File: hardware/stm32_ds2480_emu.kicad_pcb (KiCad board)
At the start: 2 copper layers, 31 x 25.5 mm, 26 parts, among them J1 USB_B_Micro, J2 SWD, J3 Pull-Up, J4 OW, Q1 SI2302CDS, SW1 BOOT, U1 AP2204K-3.3, U2 STM32F042F6Px

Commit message: Firmware added
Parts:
- moved J2 7.58 mm to (129.0, 95.2), turned to 270 degrees
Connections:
- J2 pad 2: /SYS_SWCLK -> /SYS_SWDIO
- J2 pad 3: /SYS_SWDIO -> /SYS_SWCLK
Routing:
- net +3V3: track 56.1 -> 52.1 mm, vias 3 -> 4
- net GND: track 86.5 -> 85.4 mm
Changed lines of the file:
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@@
     (thickness 1.6)
     (drawings 12)
-    (tracks 175)
+    (tracks 174)
     (zones 0)
     (modules 26)
@@
   )
   (module Connector_PinHeader_2.54mm:PinHeader_1x04_P2.54mm_Vertical placed (layer F.Cu)
-    (at 121.42 95.25 90)
+    (at 129 95.25 270)
     (descr "Through hole straight pin header, 1x04, 2.54mm pitch, single row")
     (tags "Through hole pin header THT 1x04 2.54mm single row")
-    (fp_text reference J2 (at 0 -2.33 90) (layer F.SilkS) hide
-      (effects (font (size 1 1) (thickness 0.15)))
-    )
-    (fp_text value SWD (at 0 9.95 90) (layer F.Fab) hide
-      (effects (font (size 1 1) (thickness 0.15)))
-    )
-    (fp_text user %R (at 0 3.81 180) (layer F.Fab)
+    (fp_text reference J2 (at 0 -2.33 270) (layer F.SilkS) hide
+      (effects (font (size 1 1) (thickness 0.15)))
+    )
+    (fp_text value SWD (at 0 9.95 270) (layer F.Fab) hide
+      (effects (font (size 1 1) (thickness 0.15)))
+    )
+    (fp_text user %R (at 0 3.81) (layer F.Fab)
       (effects (font (size 1 1) (thickness 0.15)))
     )
@@
     (fp_line (start 1.27 -1.27) (end 1.27 8.89) (layer F.Fab) (width 0.1))
     (fp_line (start -0.635 -1.27) (end 1.27 -1.27) (layer F.Fab) (width 0.1))
-    (pad 4 thru_hole oval (at 0 7.62 90) (size 1.7 1.7) (drill 1) (layers *.Cu *.Mask)
-      (net 2 GND))
-    (pad 3 thru_hole oval (at 0 5.08 90) (size 1.7 1.7) (drill 1) (layers *.Cu *.Mask)
+    (pad 4 thru_hole oval (at 0 7.62 270) (size 1.7 1.7) (drill 1) (layers *.Cu *.Mask)
+      (net 2 GND))
+    (pad 3 thru_hole oval (at 0 5.08 270) (size 1.7 1.7) (drill 1) (layers *.Cu *.Mask)
+      (net 9 /SYS_SWCLK))
+    (pad 2 thru_hole oval (at 0 2.54 270) (size 1.7 1.7) (drill 1) (layers *.Cu *.Mask)
       (net 10 /SYS_SWDIO))
-    (pad 2 thru_hole oval (at 0 2.54 90) (size 1.7 1.7) (drill 1) (layers *.Cu *.Mask)
-      (net 9 /SYS_SWCLK))
-    (pad 1 thru_hole rect (at 0 0 90) (size 1.7 1.7) (drill 1) (layers *.Cu *.Mask)
+    (pad 1 thru_hole rect (at 0 0 270) (size 1.7 1.7) (drill 1) (layers *.Cu *.Mask)
       (net 3 +3V3))
     (model ${KISYS3DMOD}/Connector_PinHeader_2.54mm.3dshapes/PinHeader_1x04_P2.54mm_Vertical.wrl
@@
   (segment (start 122.47 87.53) (end 122.4125 87.5875) (width 0.25) (layer B.Cu) (net 2))
   (segment (start 122.47 86) (end 122.47 87.53) (width 0.25) (layer B.Cu) (net 2) (status 10))
-  (segment (start 122.4125 87.5875) (end 119.6625 87.5875) (width 0.25) (layer B.Cu) (net 2))
   (segment (start 124.25 87.5875) (end 122.4125 87.5875) (width 0.25) (layer B.Cu) (net 2) (status 10))
   (via (at 121.5 78) (size 0.8) (drill 0.4) (layers F.Cu B.Cu) (net 2))
@@
   (segment (start 133.8125 86.2625) (end 133.8 86.25) (width 0.25) (layer F.Cu) (net 2) (status 30))
   (segment (start 133.8125 88) (end 133.8125 86.2625) (width 0.25) (layer F.Cu) (net 2) (status 30))
-  (segment (start 133 95.25) (end 129.04 95.25) (width 0.25) (layer F.Cu) (net 2) (status 20))
-  (segment (start 133.8125 94.4375) (end 133 95.25) (width 0.25) (layer F.Cu) (net 2))
   (segment (start 133.775 90.75) (end 133.8125 90.7125) (width 0.25) (layer F.Cu) (net 2))
   (segment (start 132.7875 90.75) (end 133.775 90.75) (width 0.25) (layer F.Cu) (net 2) (status 10))
-  (segment (start 133.8125 90.7125) (end 133.8125 94.4375) (width 0.25) (layer F.Cu) (net 2))
   (segment (start 133.8125 88) (end 133.8125 90.7125) (width 0.25) (layer F.Cu) (net 2) (status 10))
   (via (at 132.5 88) (size 0.8) (drill 0.4) (layers F.Cu B.Cu) (net 2))
@@
   (segment (start 124.5 77.1) (end 131.1 77.1) (width 0.25) (layer B.Cu) (net 2))
   (segment (start 122.4 77.1) (end 124.5 77.1) (width 0.25) (layer B.Cu) (net 2))
-  (segment (start 121.42 90.82) (end 121.35 90.75) (width 0.65) (layer F.Cu) (net 3) (status 30))
-  (segment (start 121.42 95.25) (end 121.42 90.82) (width 0.65) (layer F.Cu) (net 3) (status 30))
+  (segment (start 121.38 87.595) (end 121.3875 87.5875) (width 0.25) (layer B.Cu) (net 2))
+  (segment (start 121.38 95.25) (end 121.38 87.595) (width 0.25) (layer B.Cu) (net 2) (status 10))
+  (segment (start 121.3875 87.5875) (end 119.6625 87.5875) (width 0.25) (layer B.Cu) (net 2))
+  (segment (start 122.4125 87.5875) (end 121.3875 87.5875) (width 0.25) (layer B.Cu) (net 2))
   (segment (start 121.4875 74.8) (end 121.5 74.8125) (width 0.65) (layer F.Cu) (net 3) (status 30))
   (segment (start 119.6 74.8) (end 121.4875 74.8) (width 0.65) (layer F.Cu) (net 3) (status 30))
@@
   (segment (start 124.25001 84.799996) (end 124.250006 84.8) (width 0.65) (layer B.Cu) (net 3))
   (segment (start 126.5 84.799996) (end 124.25001 84.799996) (width 0.65) (layer B.Cu) (net 3))
-  (segment (start 130.049996 84.799996) (end 130.1 84.85) (width 0.65) (layer B.Cu) (net 3))
-  (segment (start 126.5 84.799996) (end 130.049996 84.799996) (width 0.65) (layer B.Cu) (net 3))
-  (segment (start 130.1 78) (end 130.1 84.85) (width 0.65) (layer B.Cu) (net 3))
-  (segment (start 121.42 92.58) (end 121.42 95.25) (width 0.65) (layer B.Cu) (net 3) (status 20))
-  (segment (start 130.1 84.85) (end 130.1 88.8) (width 0.65) (layer B.Cu) (net 3))
-  (segment (start 130.1 88.8) (end 128.15 90.75) (width 0.65) (layer B.Cu) (net 3))
-  (segment (start 128.15 90.75) (end 123.25 90.75) (width 0.65) (layer B.Cu) (net 3))
-  (segment (start 123.25 90.75) (end 121.42 92.58) (width 0.65) (layer B.Cu) (net 3))
   (segment (start 129.9625 84.825) (end 130.1 84.6875) (width 0.25) (layer F.Cu) (net 3) (status 30))
   (segment (start 128.2 84.825) (end 129.9625 84.825) (width 0.25) (layer F.Cu) (net 3) (status 30))
+  (via (at 122.95 90.75) (size 0.8) (drill 0.4) (layers F.Cu B.Cu) (net 3))
+  (segment (start 121.35 90.75) (end 122.95 90.75) (width 0.65) (layer F.Cu) (net 3) (status 10))
+  (segment (start 129 90.75) (end 129 95.25) (width 0.65) (layer B.Cu) (net 3) (status 20))
+  (segment (start 122.95 90.75) (end 129 90.75) (width 0.65) (layer B.Cu) (net 3))
+  (segment (start 129 79.1) (end 130.1 78) (width 0.65) (layer B.Cu) (net 3))
+  (segment (start 128.999996 84.799996) (end 129 84.8) (width 0.65) (layer B.Cu) (net 3))
+  (segment (start 126.5 84.799996) (end 128.999996 84.799996) (width 0.65) (layer B.Cu) (net 3))
+  (segment (start 129 84.8) (end 129 79.1) (width 0.65) (layer B.Cu) (net 3))
+  (segment (start 129 90.75) (end 129 84.8) (width 0.65) (layer B.Cu) (net 3))
   (segment (start 118.050001 85.175) (end 118.525 85.175) (width 0.25) (layer F.Cu) (net 4))
   (via (at 118.8 85.45) (size 0.8) (drill 0.4) (layers F.Cu B.Cu) (net 4))
@@
   (segment (start 133.8125 80.5) (end 133.8125 79.1) (width 0.25) (layer F.Cu) (net 8) (status 20))
   (segment (start 132.1 80.5) (end 133.8125 80.5) (width 0.25) (layer F.Cu) (net 8) (status 10))
-  (segment (start 123.96 88.21) (end 123.96 95.25) (width 0.25) (layer F.Cu) (net 9) (status 20))
-  (segment (start 123.175 87.425) (end 123.96 88.21) (width 0.25) (layer F.Cu) (net 9))
   (segment (start 122.3 87.425) (end 123.175 87.425) (width 0.25) (layer F.Cu) (net 9) (status 10))
-  (segment (start 126.5 88.5) (end 126.5 95.25) (width 0.25) (layer F.Cu) (net 10) (status 20))
-  (segment (start 124.775 86.775) (end 126.5 88.5) (width 0.25) (layer F.Cu) (net 10))
-  (segment (start 122.3 86.775) (end 124.775 86.775) (width 0.25) (layer F.Cu) (net 10) (status 10))
+  (segment (start 123.92 88.17) (end 123.175 87.425) (width 0.25) (layer F.Cu) (net 9))
+  (segment (start 123.92 95.25) (end 123.92 88.17) (width 0.25) (layer F.Cu) (net 9) (status 10))
+  (segment (start 124.775 86.775) (end 122.3 86.775) (width 0.25) (layer F.Cu) (net 10) (status 20))
+  (segment (start 126.46 88.46) (end 124.775 86.775) (width 0.25) (layer F.Cu) (net 10))
+  (segment (start 126.46 95.25) (end 126.46 88.46) (width 0.25) (layer F.Cu) (net 10) (status 10))
   (segment (start 136.9 82.5) (end 138.4 84) (width 0.25) (layer F.Cu) (net 11))
   (segment (start 135.6875 82.5) (end 136.9 82.5) (width 0.25) (layer F.Cu) (net 11) (status 10))

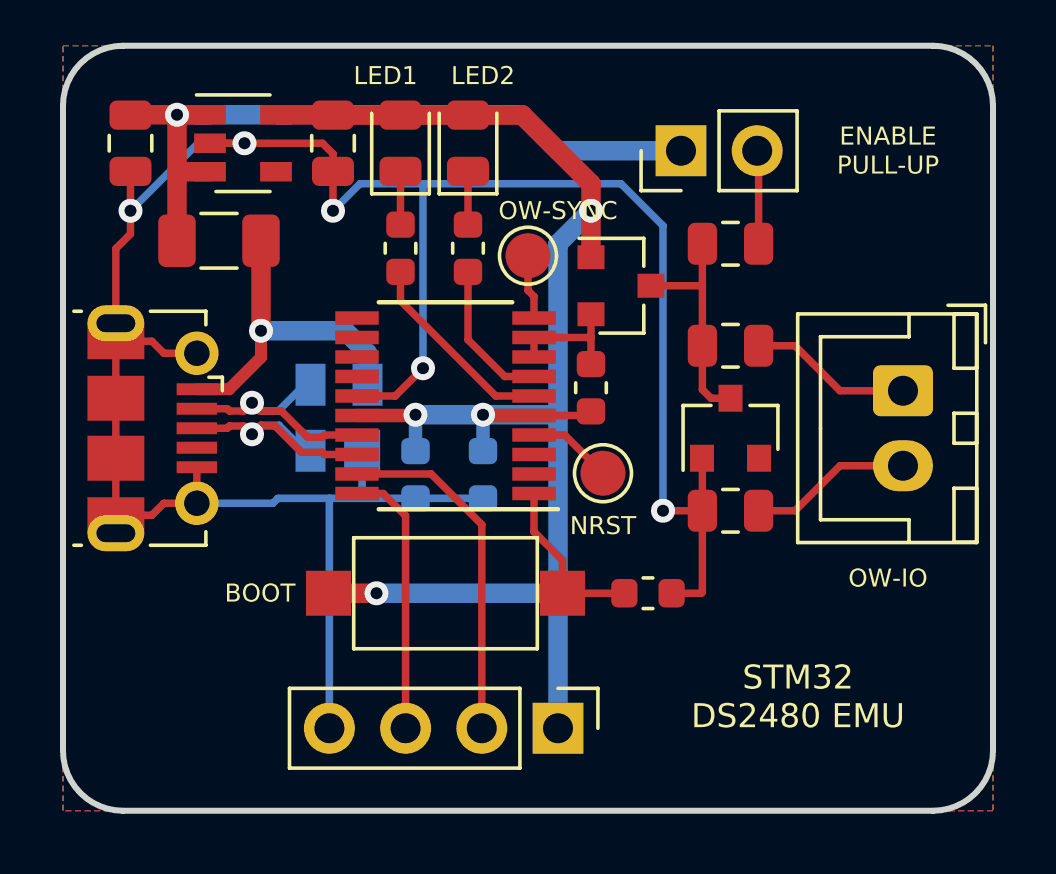
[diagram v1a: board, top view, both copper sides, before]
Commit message: All componenets moved to top side
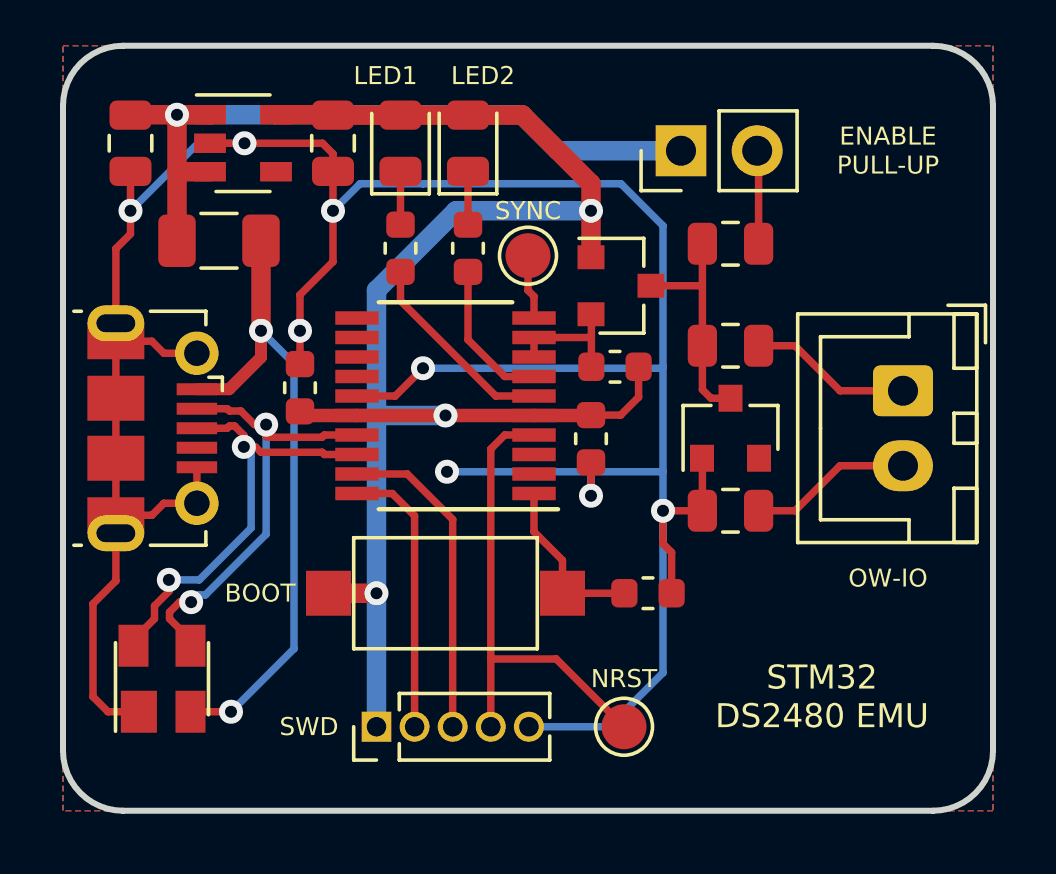
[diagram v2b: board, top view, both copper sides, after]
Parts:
- removed the J2 at (129.0, 95.2)
- added J4: SWD, Connector_PinHeader_1.27mm:PinHeader_1x05_P1.27mm_Vertical, F.Cu at (123.0, 95.2)
- C3, C4: moved to F.Cu
- D4: renamed from D1; moved to F.Cu
- TP1: renamed from TP2; value OW-SYNC -> SYNC
- moved D4 10.5 mm to (115.8, 93.6)
- moved TP2 8.48 mm to (131.2, 95.2)
- moved C3 4.82 mm to (120.4, 83.9), turned to 90 degrees
- moved C4 3.79 mm to (130.1, 85.6)
- moved R5 1.06 mm to (130.9, 83.2), turned to 180 degrees
- renumbered D2 to D1, D3 to D2, D4 to D3, J3 to J1, J4 to J2, J1 to J3, R7 to R1, R5 to R4, R4 to R5, R1 to R7, TP1 to TP2
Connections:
- net Net-(TP1-Pad1) renamed /NRST
- D4 pad 2: /USB_P -> Net-(D4-Pad2)
- D4 pad 4: Net-(D1-Pad4) -> /USB_P
- F1 pad 2: Net-(D1-Pad4) -> Net-(D4-Pad2)
- J3 pad 1: Net-(D1-Pad4) -> Net-(D4-Pad2)
- J3 pad 4: (no net) -> Net-(J3-Pad4)
- U1 pad 4: (no net) -> Net-(U1-Pad4)
- U2 pad 11: (no net) -> Net-(U2-Pad11)
- U2 pad 12: (no net) -> Net-(U2-Pad12)
- U2 pad 13: (no net) -> Net-(U2-Pad13)
- U2 pad 14: (no net) -> Net-(U2-Pad14)
- U2 pad 2: (no net) -> Net-(U2-Pad2)
- U2 pad 3: (no net) -> Net-(U2-Pad3)
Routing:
- net Net-(D4-Pad2): track 0.00 -> 21.8 mm, vias 0 -> 2
- net GND: track 85.4 -> 100.9 mm, vias 5 -> 8
- net /NRST: track 2.83 -> 16.3 mm
- net Net-(D1-Pad4): track 11.4 -> 0.00 mm, vias 1 -> 0
- net /USB_N: track 8.42 -> 15.4 mm, vias 1 -> 2
- net /USB_P: track 8.42 -> 14.9 mm, vias 1 -> 2
- net +3V3: track 52.1 -> 53.2 mm, vias 4 -> 3
- net /SYS_SWDIO: track 11.6 -> 10.7 mm

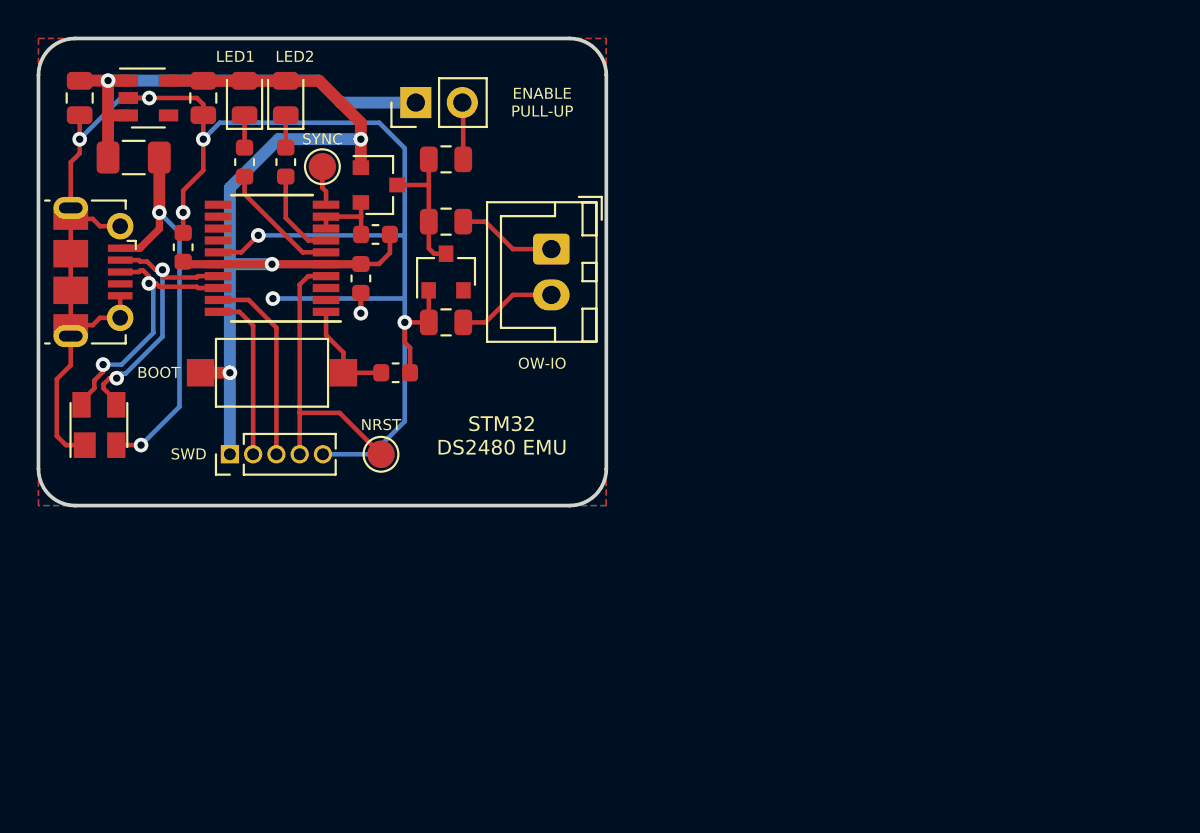
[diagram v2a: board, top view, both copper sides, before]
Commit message: New USB stick PCB design
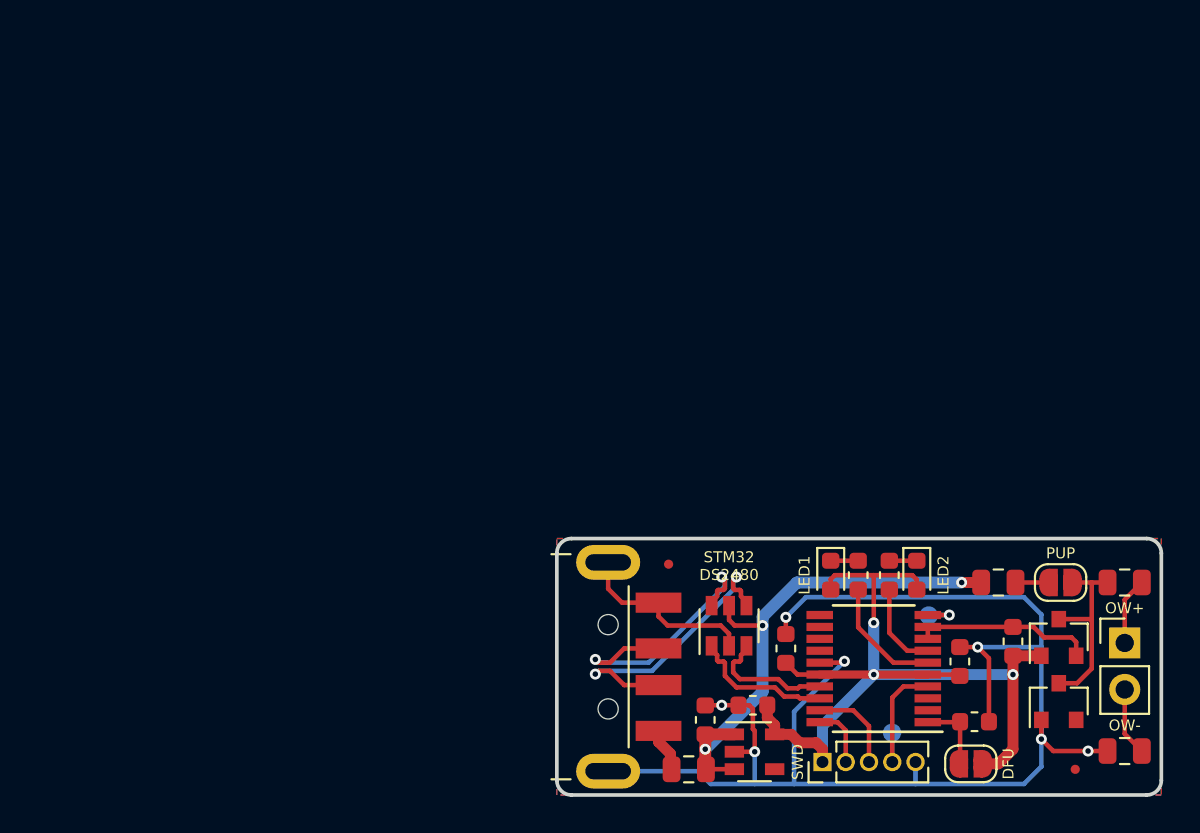
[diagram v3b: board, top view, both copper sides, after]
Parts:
- removed the C2 at (121.5, 75.8)
- removed D4: SP0503BAHT, Package_TO_SOT_SMD:SOT-143
- removed J4: SWD, Connector_PinHeader_1.27mm:PinHeader_1x05_P1.27mm_Vertical
- removed the R1 at (134.8, 79.1)
- removed the R6 at (134.8, 88.0)
- removed SW1: BOOT, Button_Switch_SMD:SW_SPST_CK_RS282G05A3
- added C4: 1uF, Capacitor_SMD:C_0603_1608Metric, F.Cu at (148.9, 109.7)
- added FID1: Fiducial, Fiducial:Fiducial_0.5mm_Mask1.5mm, F.Cu at (146.9, 101.2)
- added FID2: Fiducial, Fiducial:Fiducial_0.5mm_Mask1.5mm, F.Cu at (169.1, 112.4)
- added JP1: PUP, Jumper:SolderJumper-2_P1.3mm_Open_RoundedPad1.0x1.5mm, F.Cu at (168.3, 102.2)
- added JP2: DFU, Jumper:SolderJumper-2_P1.3mm_Open_RoundedPad1.0x1.5mm, F.Cu at (163.4, 112.1)
- added R2: 100R, Resistor_SMD:R_0603_1608Metric, F.Cu at (158.9, 101.8)
- added R7: 4.7R, Resistor_SMD:R_0805_2012Metric, F.Cu at (171.8, 111.4)
- added U3: AP2204K-3.3, Package_TO_SOT_SMD:SOT-23-5, F.Cu at (151.6, 111.4)
- C1: value 1uF -> 100nF; footprint Capacitor_SMD:C_0805_2012Metric -> Capacitor_SMD:C_0603_1608Metric
- C3: value 100nF -> 2.2uF
- D1, D2: footprint LED_SMD:LED_0805_2012Metric -> LED_SMD:LED_0603_1608Metric
- F1: footprint Fuse:Fuse_1206_3216Metric -> Fuse:Fuse_0805_2012Metric
- J1: value Pull-Up -> OW
- J2: value OW -> USB_A; footprint Connector_JST:JST_XH_B02B-XH-A_1x02_P2.50mm_Vertical -> Connector_USB:USB_A_CNCTech_1001-011-01101_Horizontal
- J3: value USB_B_Micro -> SWD; footprint Connector_USB:USB_Micro-B_Molex-105017-0001 -> Connector_PinHeader_1.27mm:PinHeader_1x05_P1.27mm_Vertical
- R3: value 100R -> 2.2K; footprint Resistor_SMD:R_0603_1608Metric -> Resistor_SMD:R_0805_2012Metric
- TP1, TP2: footprint TestPoint:TestPoint_Pad_D1.5mm -> TestPoint:TestPoint_Pad_D1.0mm; moved to B.Cu
- U1: value AP2204K-3.3 -> USBLC6-2SC6; footprint Package_TO_SOT_SMD:SOT-23-5 -> Package_TO_SOT_SMD:SOT-23-6
- moved C1 48.9 mm to (153.3, 105.8), turned to 90 degrees
- moved J1 48.7 mm to (171.8, 105.5), turned to 0 degrees
- moved J3 48.0 mm to (155.3, 112.0), turned to 90 degrees
- moved R3 45.2 mm to (164.9, 102.2), turned to 0 degrees
- moved F1 45.1 mm to (148.0, 112.4), turned to 180 degrees
- moved Q1 44.6 mm to (168.2, 105.2), turned to 90 degrees
- moved D2 43.2 mm to (160.4, 101.8), turned to -90 degrees
- moved U1 42.8 mm to (150.2, 104.6), turned to 90 degrees
- moved R4 42.0 mm to (171.8, 102.2)
- moved R5 41.3 mm to (165.7, 105.4), turned to 90 degrees
- moved D1 41.3 mm to (155.8, 101.8), turned to -90 degrees
- moved TP1 41.2 mm to (161.1, 104.0)
- moved D3 40.9 mm to (168.2, 108.7)
- moved R1 40.4 mm to (157.2, 101.8)
- moved C3 39.9 mm to (151.5, 108.9), turned to 180 degrees
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- renumbered C4 to C2, R2 to R1, R7 to R6
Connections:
- net /OW-5V renamed Net-(D3-Pad1)
- C1 pad 1: +5V -> +3V3
- F1 pad 2: Net-(D4-Pad2) -> Net-(F1-Pad2)
- J1 pad 1: +5V -> Net-(J1-Pad1)
- J2 pad 1: Net-(J2-Pad1) -> Net-(F1-Pad2)
- J2 pad 2: Net-(J2-Pad2) -> /USB1_DN
- J3 pad 1: Net-(D4-Pad2) -> +3V3
- J3 pad 2: /USB_N -> /SYS_SWCLK
- J3 pad 3: /USB_P -> /SYS_SWDIO
- J3 pad 4: Net-(J3-Pad4) -> /NRST
- R3 pad 1: Net-(D2-Pad1) -> +5V
- R3 pad 2: /LED2 -> Net-(JP1-Pad1)
- R4 pad 1: Net-(J2-Pad1) -> Net-(J1-Pad1)
- U1 pad 1: +5V -> /USB_DP
- U1 pad 3: +5V -> /USB_DN
- U1 pad 4: Net-(U1-Pad4) -> /USB1_DN
- U1 pad 5: +3V3 -> +5V
- U2 pad 17: /USB_N -> /USB_DN
- U2 pad 18: /USB_P -> /USB_DP
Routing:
- net Net-(D4-Pad2): track 21.8 -> 0.00 mm, vias 2 -> 0
- net /USB1_DN: track 0.00 -> 16.1 mm, vias 0 -> 2
- net /USB1_DP: track 0.00 -> 15.4 mm, vias 0 -> 2
- net /USB_N: track 15.4 -> 0.00 mm, vias 2 -> 0
- net /USB_P: track 14.9 -> 0.00 mm, vias 2 -> 0
- net GND: track 100.9 -> 90.6 mm, vias 8 -> 7
- net /NRST: track 16.3 -> 7.32 mm
- net +5V: track 25.3 -> 33.9 mm, vias 1 -> 3
- net /USB_DP: track 0.00 -> 7.79 mm
- net /USB_DN: track 0.00 -> 7.04 mm
- net /SYS_SWCLK: track 9.26 -> 3.33 mm
- net /SYS_SWDIO: track 10.7 -> 5.01 mm
- net /OW-3V3: track 4.32 -> 9.84 mm
- net Net-(J2-Pad2): track 5.43 -> 0.00 mm
- net Net-(J2-Pad1): track 5.43 -> 0.00 mm
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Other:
- board size 31 x 25.5 mm -> 33 x 14 mm
- net class Default: via_dia 0.8 -> 0.6; via_drill 0.4 -> 0.3
- net class POWER: via_dia 0.8 -> 0.6; via_drill 0.4 -> 0.3
- board text added: "OW+"
- board text added: "OW-"
- board text added: "STM32 DS2480"
- board text removed: "BOOT"
- board text removed: "ENABLE PULL-UP"
- board text removed: "OW-IO"
- board text removed: "STM32 DS2480 EMU"
